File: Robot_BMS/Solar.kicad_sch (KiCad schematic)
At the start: 1 part, among them U8 LM3488MM

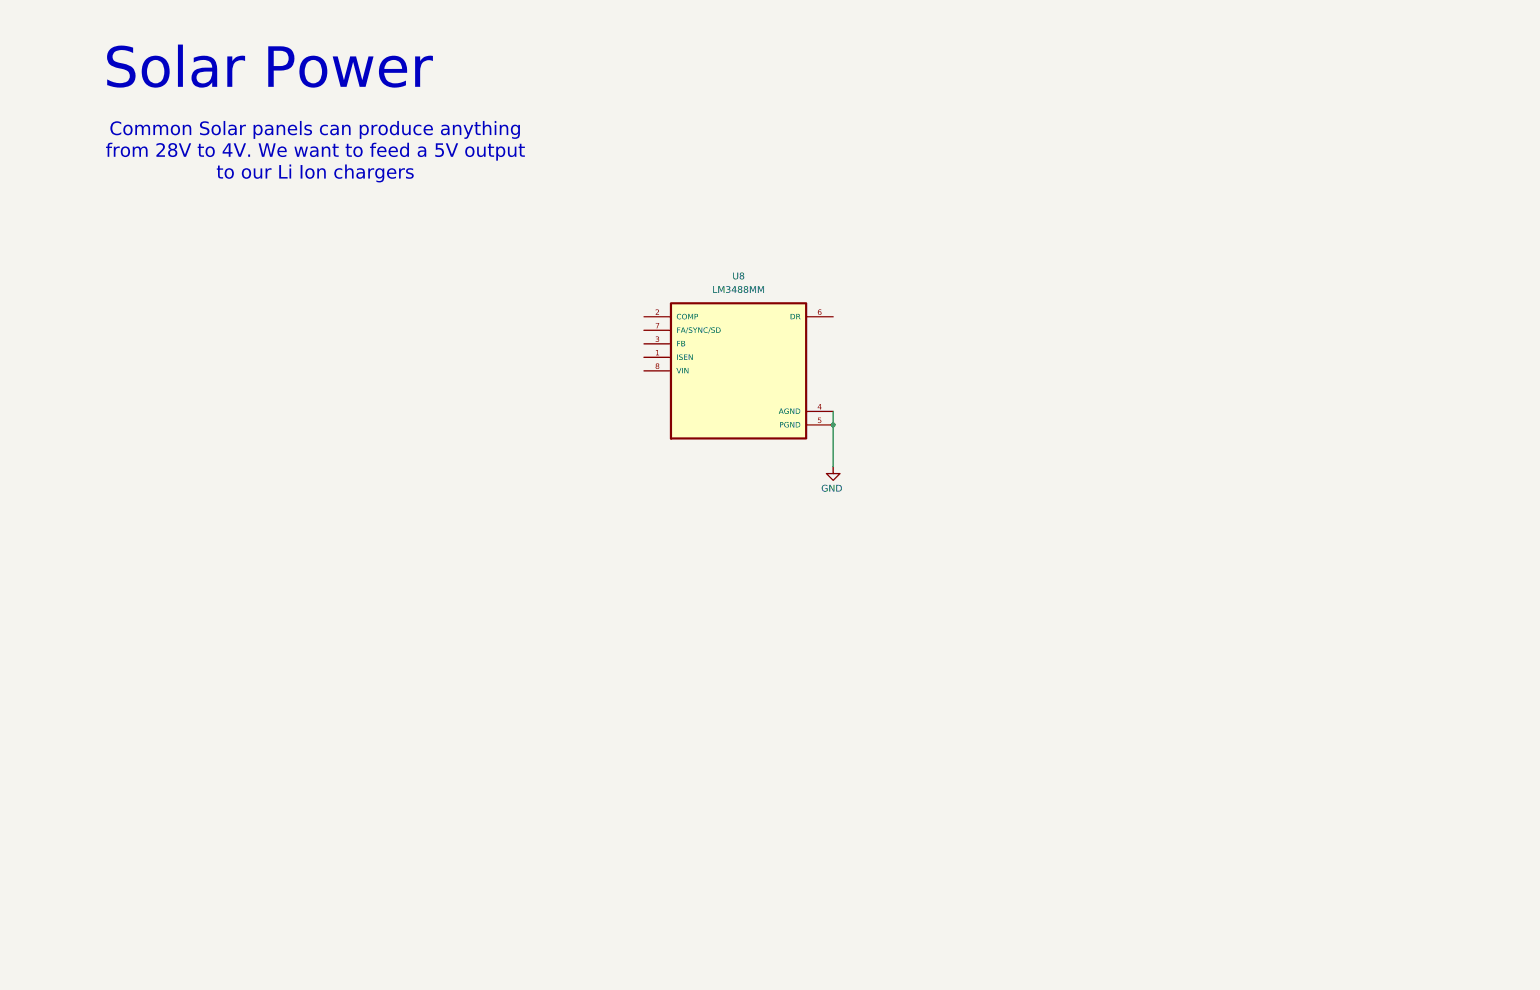
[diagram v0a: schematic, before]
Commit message: USB-c PD to 15V
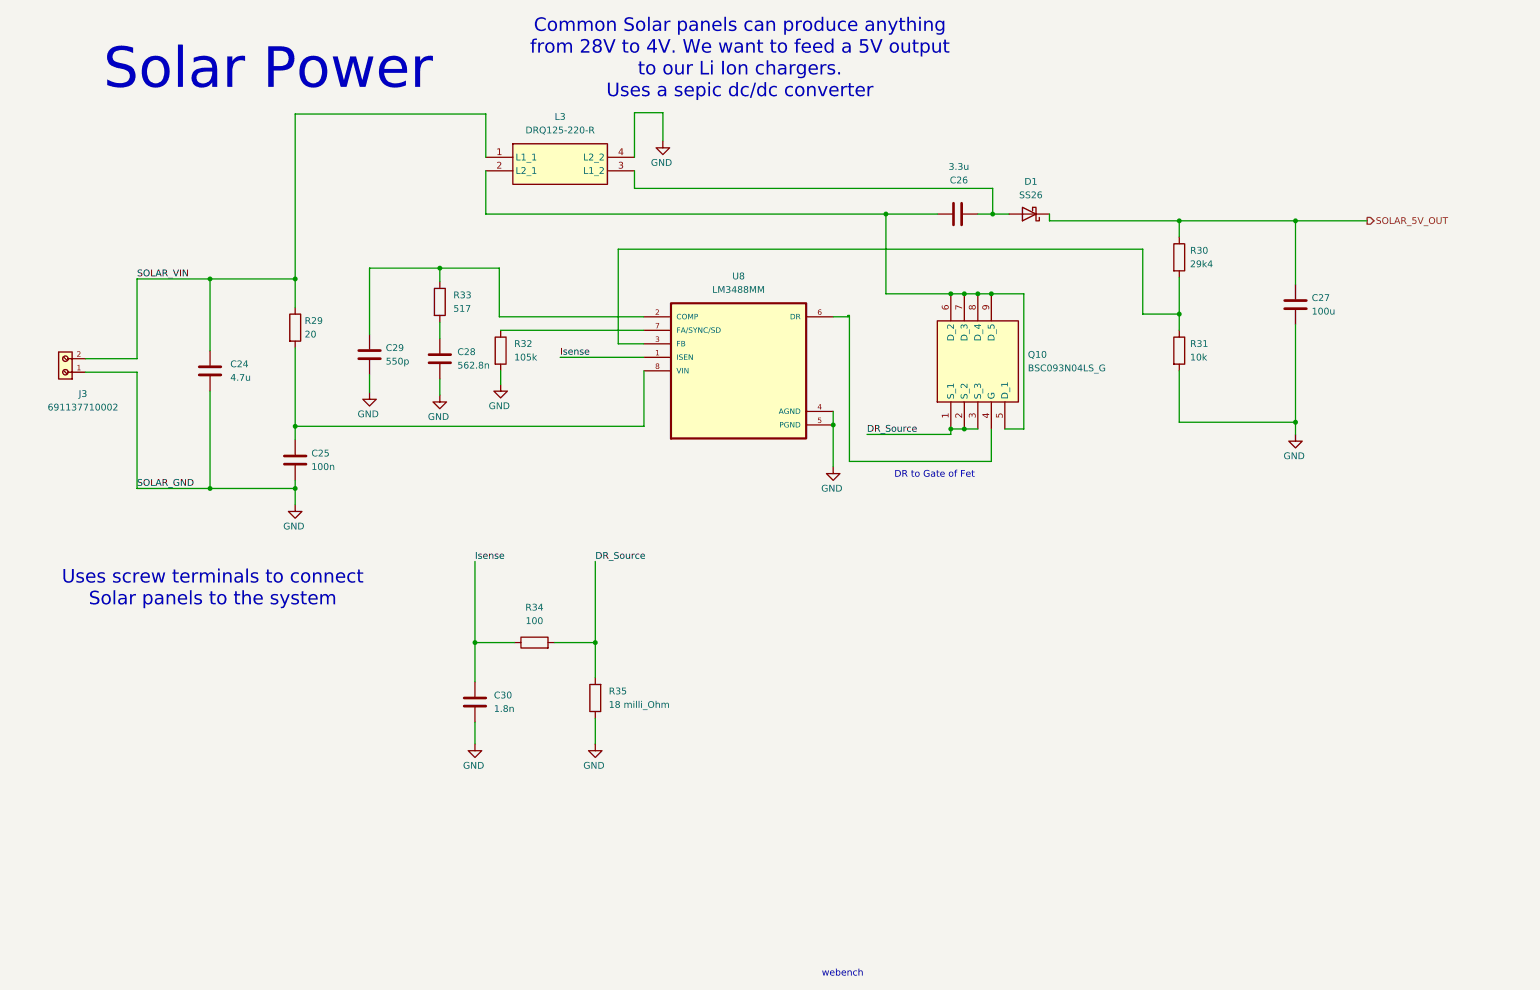
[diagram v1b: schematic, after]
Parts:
- added C24: 4.7u, symbol Device:C
- added C25: 100n, symbol Device:C
- added C26: 3.3u, symbol Device:C
- added C27: 100u, symbol Device:C
- added C28: 562.8n, symbol Device:C
- added C29: 550p, symbol Device:C
- added C30: 1.8n, symbol Device:C
- added D1: SS26, Diode_SMD:D_SMA, symbol Diode:SS26
- added J3: 691137710002, 691137710002:691137710002, symbol 691137710002-2 Terminal Connector:691137710002
- added L3: DRQ125-220-R, DRQ125220R, symbol Power Inductor DRQ125:DRQ125-220-R
- added Q10: BSC093N04LS_G, BSC120N03LSG, symbol BSC093N04LS G:BSC093N04LS_G
- added R29: 20, symbol Device:R
- added R30: 29k4, symbol Device:R
- added R31: 10k, symbol Device:R
- added R32: 105k, symbol Device:R
- added R33: 517, symbol Device:R
- added R34: 100, symbol Device:R
- added R35: 18 milli_Ohm, symbol Device:R
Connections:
- net GND: now also C24.2, C25.2, C27.2, C28.2, C29.2, C30.2, J3.1, L3.4 (L2_2), R31.2, R32.2, R35.1
- net Isense: now reaches U8.1 (ISEN)
- net Isense: now also C30.1, R34.1
- net at U8.2 (COMP): now also C29.1, R33.1
- net at U8.3 (FB): now also R30.2, R31.1
- net at U8.6 (DR): now also Q10.4 (G)
- net at U8.7 (FA/SYNC/SD): now also R32.1
- net at U8.8 (VIN): now also C25.1, R29.2
- new net: C28.1, R33.2
- new net: C26.1, D1.2 (A), L3.3 (L1_2)
- new net: C26.2, L3.2 (L2_1), Q10.5 (D_1), Q10.6 (D_2), Q10.7 (D_3), Q10.8 (D_4), Q10.9 (D_5)
- new net DR_Source: Q10.1 (S_1), Q10.2 (S_2), Q10.3 (S_3), R34.2, R35.2
- new net SOLAR_5V_OUT: C27.1, D1.1 (K), R30.1
- new net SOLAR_VIN: C24.1, J3.2, L3.1 (L1_1), R29.1
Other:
- note added: "Common Solar panels can produce anything from 28V to 4V. We want to feed a 5V output to our Li Ion chargers. Uses a sepic dc/dc converter"
- note added: "DR to Gate of Fet"
- note added: "Uses screw terminals to connect Solar panels to the system"
- note added: "webench"
- note removed: "Common Solar panels can produce anything from 28V to 4V. We want to feed a 5V output to our Li Ion chargers"

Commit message: solar charger set to 15V
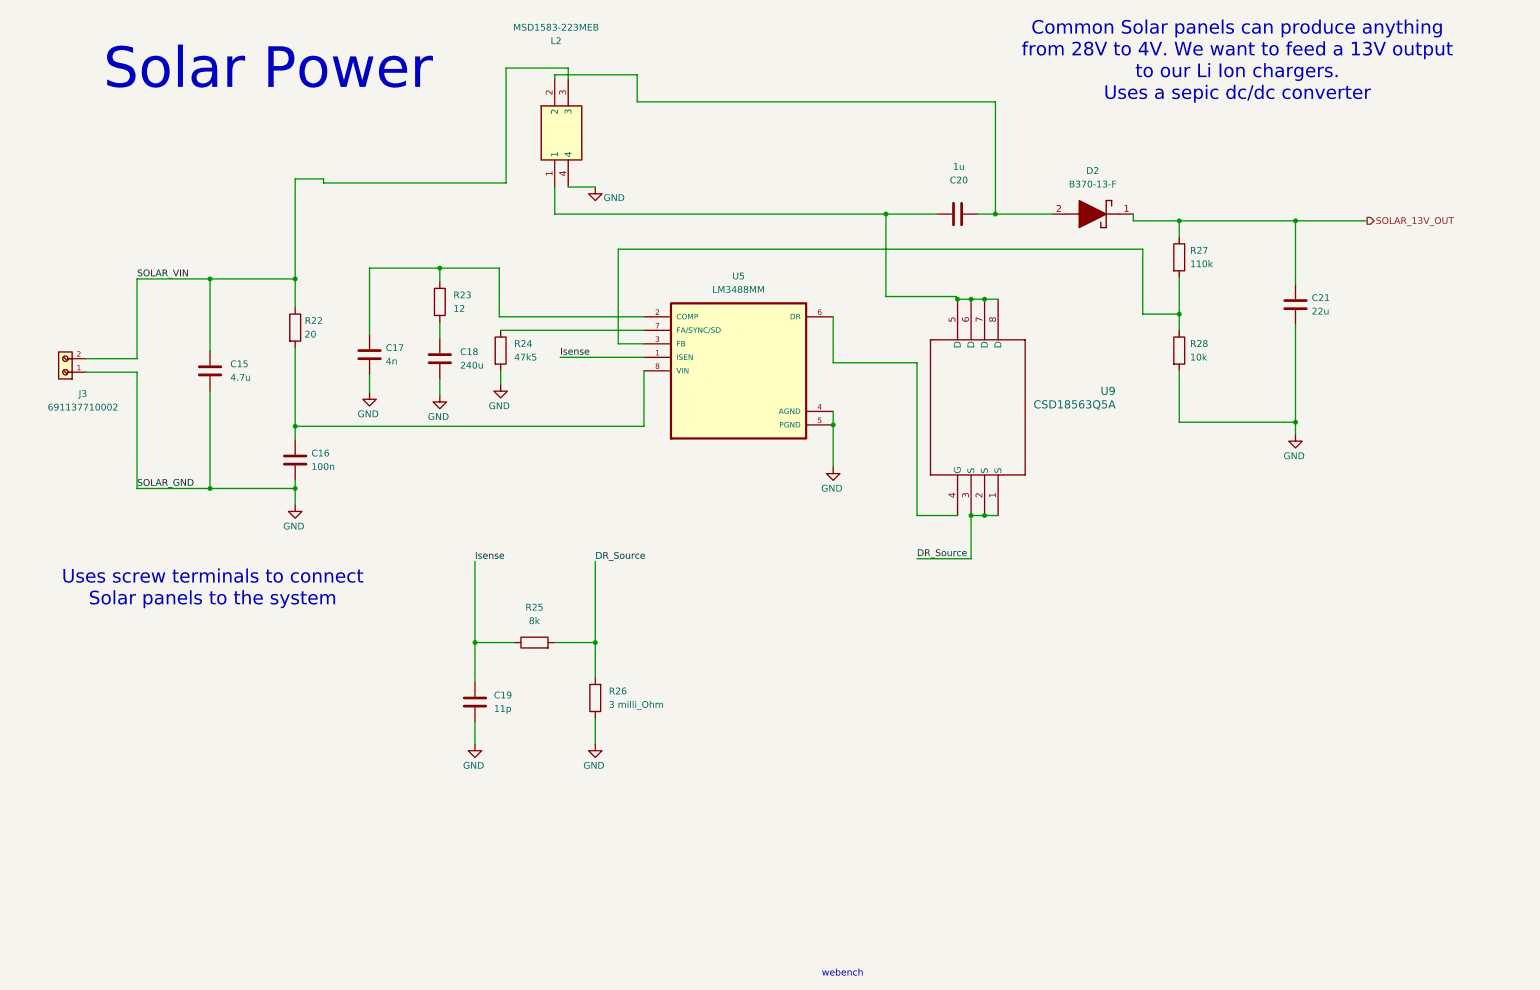
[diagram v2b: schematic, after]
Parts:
- removed D1: SS26, Diode_SMD:D_SMA, symbol Diode:SS26
- removed L3: DRQ125-220-R, DRQ125220R, symbol Power Inductor DRQ125:DRQ125-220-R
- removed Q10: BSC093N04LS_G, BSC120N03LSG, symbol BSC093N04LS G:BSC093N04LS_G
- added D2: B370-13-F, DIOM7959X250N, symbol B370-13-F:B370-13-F
- added L2: MSD1583-223MEB, MSD1583223MEB, symbol MSD1583-223MEB:MSD1583-223MEB
- added U9: CSD18563Q5A, DQJ8, symbol CSD18563Q5A:CSD18563Q5A
- C17: renamed from C29; value 550p -> 4n
- C18: renamed from C28; value 562.8n -> 240u
- C19: renamed from C30; value 1.8n -> 11p
- C20: renamed from C26; value 3.3u -> 1u
- C21: renamed from C27; value 100u -> 22u
- R23: renamed from R33; value 517 -> 12
- R24: renamed from R32; value 105k -> 47k5
- R25: renamed from R34; value 100 -> 8k
- R26: renamed from R35; value 18 milli_Ohm -> 3 milli_Ohm
- R27: renamed from R30; value 29k4 -> 110k
- renumbered C24 to C15, C25 to C16, R29 to R22, R31 to R28, U8 to U5
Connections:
- net DR_Source: now also U9.1 (S), U9.2 (S), U9.3 (S)
- net GND: now also L2.4
- net SOLAR_VIN: now also L2.3
- net at U5.6 (DR): now also U9.4 (G)
- net at C20.1: now also D2.2 (A), L2.2
- net at C20.2: now also L2.1, U9.5 (D), U9.6 (D), U9.7 (D), U9.8 (D)
- net SOLAR_5V_OUT renamed SOLAR_13V_OUT
- net SOLAR_13V_OUT: now also D2.1 (K)
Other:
- note added: "Common Solar panels can produce anything from 28V to 4V. We want to feed a 13V output to our Li Ion chargers. Uses a sepic dc/dc converter"
- note removed: "Common Solar panels can produce anything from 28V to 4V. We want to feed a 5V output to our Li Ion chargers. Uses a sepic dc/dc converter"
- note removed: "DR to Gate of Fet"
